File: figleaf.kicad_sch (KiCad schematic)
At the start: 0 parts

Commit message: testing llmd mcu
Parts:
- added J1: nRF52840_Connect_Kit, symbol kekw:nRF52840_Connect_Kit
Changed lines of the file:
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@@
 	(generator_version "9.0")
 	(paper "A4")
+	(symbol
+		(lib_id "kekw:nRF52840_Connect_Kit")
+		(at 166.37 91.44 0)
+		(unit 1)
+		(exclude_from_sim no)
+		(in_bom yes)
+		(on_board yes)
+		(dnp no)
+		(fields_autoplaced yes)
+		(property "Reference" "J1"
+			(at 166.37 35.56 0)
+			(effects
+				(font
+					(size 1.27 1.27)
+				)
+			)
+		)
+		(property "Value" "nRF52840_Connect_Kit"
+			(at 166.37 38.1 0)
+			(effects
+				(font
+					(size 1.27 1.27)
+				)
+			)
+		)
+		(property "Footprint" ""
+			(at 166.37 91.44 0)
+			(effects
+				(font
+					(size 1.27 1.27)
+				)
+				(hide yes)
+			)
+		)
+		(property "Datasheet" ""
+			(at 166.37 91.44 0)
+			(effects
+				(font
+					(size 1.27 1.27)
+				)
+				(hide yes)
+			)
+		)
+		(property "Description" "nRF52840 Connect Kit 2x20 Header"
+			(at 166.37 91.44 0)
+			(effects
+				(font
+					(size 1.27 1.27)
+				)
+				(hide yes)
+			)
+		)
+		(pin "40"
+		)
+		(pin "14"
+		)
+		(pin "3"
+		)
+		(pin "7"
+		)
+		(pin "15"
+		)
+		(pin "17"
+		)
+		(pin "20"
+		)
+		(pin "30"
+		)
+		(pin "1"
+		)
+		(pin "10"
+		)
+		(pin "12"
+		)
+		(pin "16"
+		)
+		(pin "11"
+		)
+		(pin "39"
+		)
+		(pin "10"
+		)
+		(pin "38"
+		)
+		(pin "6"
+		)
+		(pin "4"
+		)
+		(pin "18"
+		)
+		(pin "2"
+		)
+		(pin "8"
+		)
+		(pin "9"
+		)
+		(pin "13"
+		)
+		(pin "5"
+		)
+		(pin "19"
+		)
+		(pin "37"
+		)
+		(pin "35"
+		)
+		(pin "34"
+		)
+		(pin "36"
+		)
+		(pin "33"
+		)
+		(pin "32"
+		)
+		(pin "31"
+		)
+		(pin "28"
+		)
+		(pin "29"
+		)
+		(pin "22"
+		)
+		(pin "25"
+		)
+		(pin "24"
+		)
+		(pin "26"
+		)
+		(pin "23"
+		)
+		(pin "27"
+		)
+		(pin "21"
+		)
+		(instances
+			(project ""
+				(path "/fd9c0cf8-91e7-46bd-8f73-27ef3bc34e44"
+					(reference "J1")
+					(unit 1)
+				)
+			)
+		)
+	)
 	(sheet_instances
 		(path "/"

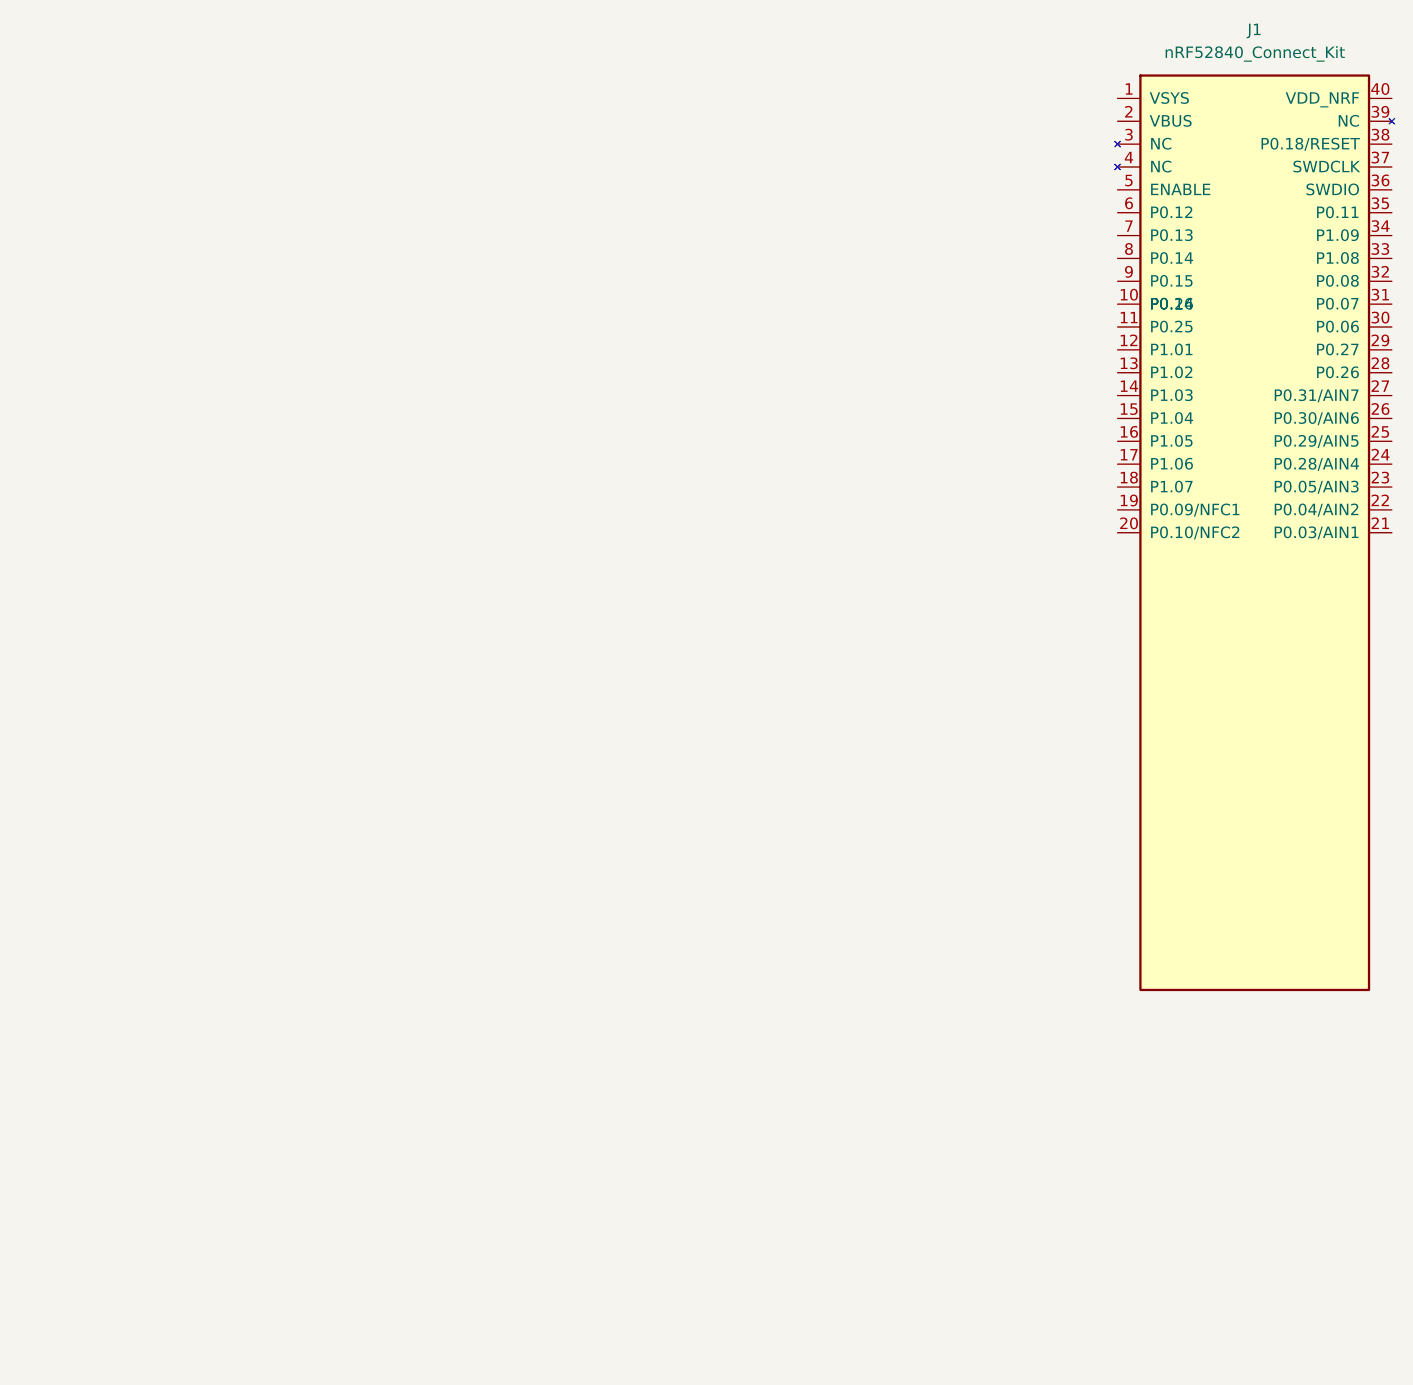
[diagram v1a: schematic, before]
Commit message: Add proper MCU symbol
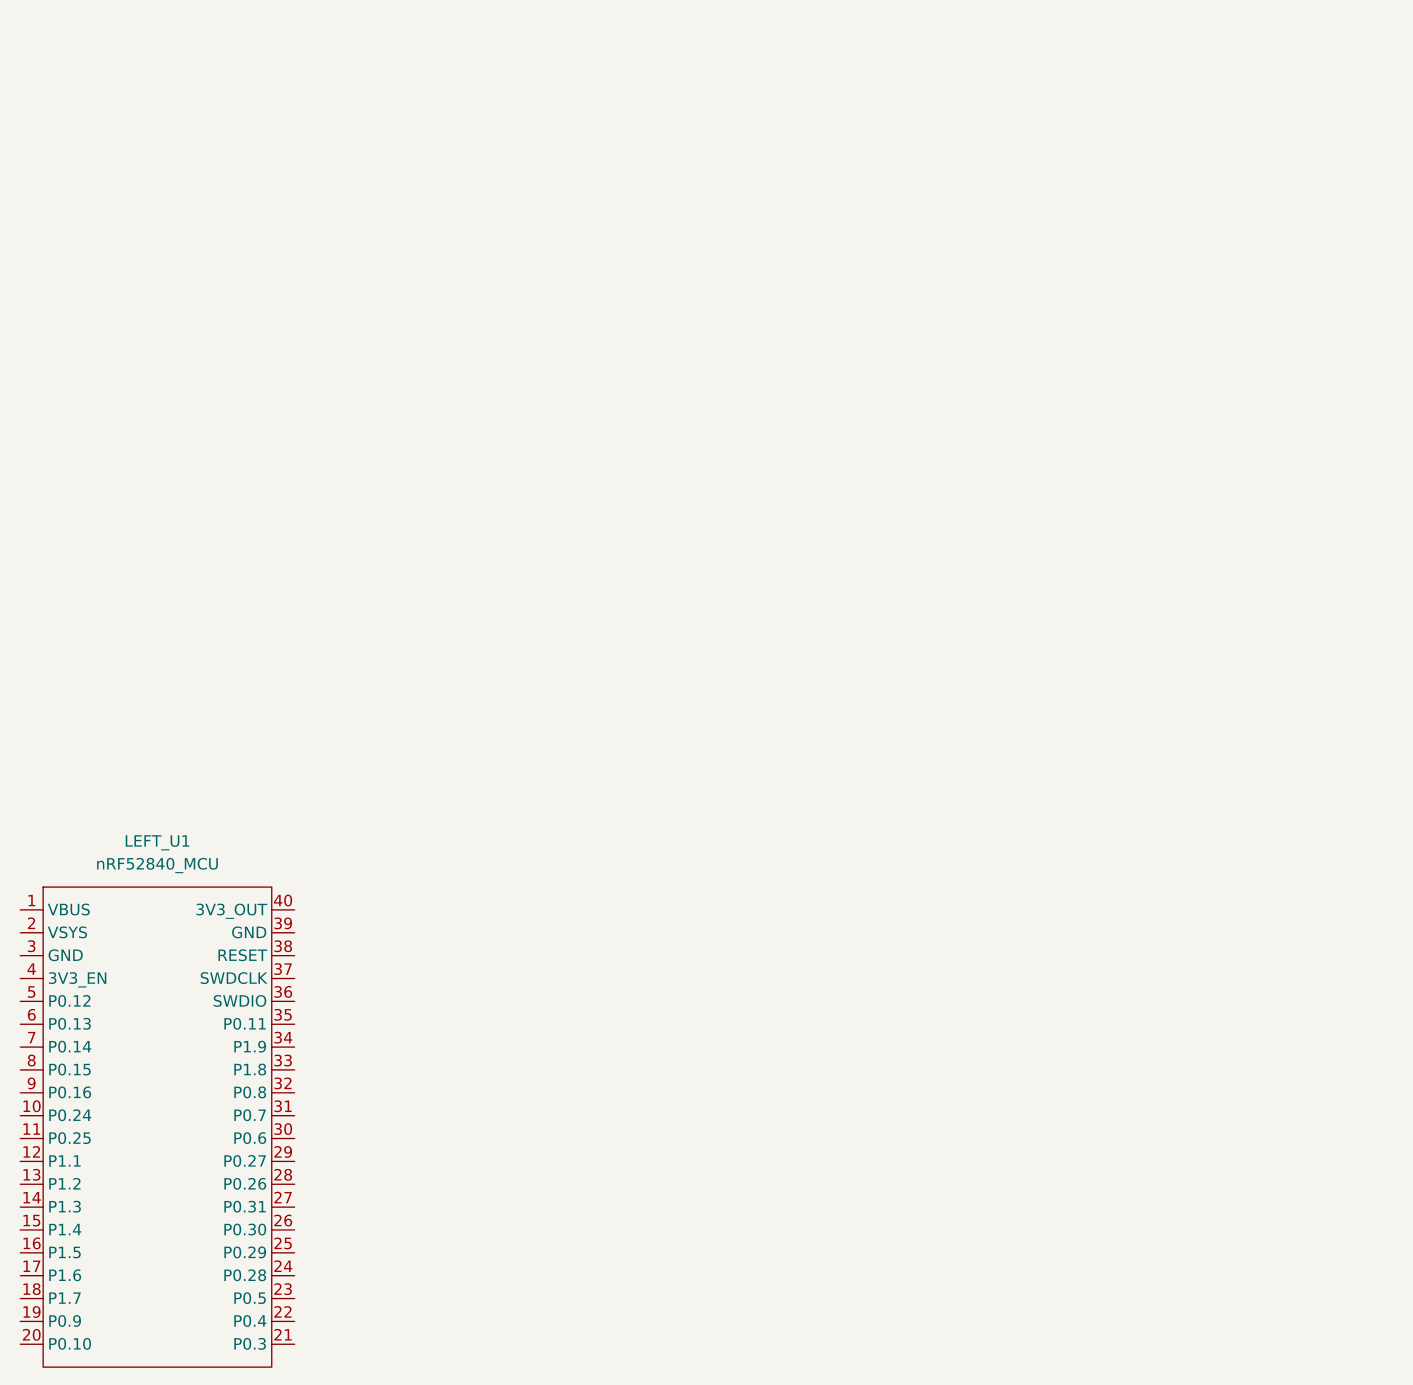
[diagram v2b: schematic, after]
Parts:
- removed J1: nRF52840_Connect_Kit, symbol kekw:nRF52840_Connect_Kit
- added LEFT_U1: nRF52840_MCU, symbol 0_graz_symbols:nRF52840_MCU
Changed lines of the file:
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@@
 	(paper "A4")
 	(symbol
-		(lib_id "kekw:nRF52840_Connect_Kit")
-		(at 166.37 91.44 0)
+		(lib_id "0_graz_symbols:nRF52840_MCU")
+		(at 44.45 158.75 0)
 		(unit 1)
 		(exclude_from_sim no)
@@
 		(dnp no)
 		(fields_autoplaced yes)
-		(property "Reference" "J1"
-			(at 166.37 35.56 0)
+		(property "Reference" "LEFT_U1"
+			(at 44.45 125.73 0)
 			(effects
 				(font
@@
 			)
 		)
-		(property "Value" "nRF52840_Connect_Kit"
-			(at 166.37 38.1 0)
+		(property "Value" "nRF52840_MCU"
+			(at 44.45 128.27 0)
 			(effects
 				(font
@@
 		)
 		(property "Footprint" ""
-			(at 166.37 91.44 0)
+			(at 44.45 158.75 0)
 			(effects
 				(font
@@
 		)
 		(property "Datasheet" ""
-			(at 166.37 91.44 0)
+			(at 44.45 158.75 0)
 			(effects
 				(font
@@
 			)
 		)
-		(property "Description" "nRF52840 Connect Kit 2x20 Header"
-			(at 166.37 91.44 0)
+		(property "Description" ""
+			(at 44.45 158.75 0)
 			(effects
 				(font
@@
 			)
 		)
-		(pin "40"
+		(pin "24"
+		)
+		(pin "31"
+		)
+		(pin "16"
+		)
+		(pin "28"
+		)
+		(pin "27"
+		)
+		(pin "25"
+		)
+		(pin "35"
+		)
+		(pin "39"
+		)
+		(pin "19"
 		)
 		(pin "14"
 		)
-		(pin "3"
+		(pin "20"
 		)
-		(pin "7"
+		(pin "40"
 		)
 		(pin "15"
@@
 		(pin "17"
 		)
-		(pin "20"
-		)
-		(pin "30"
-		)
-		(pin "1"
-		)
-		(pin "10"
-		)
-		(pin "12"
-		)
-		(pin "16"
-		)
-		(pin "11"
-		)
-		(pin "39"
-		)
-		(pin "10"
+		(pin "13"
 		)
 		(pin "38"
 		)
-		(pin "6"
-		)
-		(pin "4"
-		)
-		(pin "18"
-		)
-		(pin "2"
-		)
-		(pin "8"
-		)
-		(pin "9"
-		)
-		(pin "13"
-		)
-		(pin "5"
-		)
-		(pin "19"
+		(pin "34"
 		)
 		(pin "37"
-		)
-		(pin "35"
-		)
-		(pin "34"
 		)
 		(pin "36"
@@
 		(pin "32"
 		)
-		(pin "31"
+		(pin "18"
 		)
-		(pin "28"
+		(pin "30"
 		)
 		(pin "29"
-		)
-		(pin "22"
-		)
-		(pin "25"
-		)
-		(pin "24"
 		)
 		(pin "26"
@@
 		(pin "23"
 		)
-		(pin "27"
+		(pin "21"
 		)
-		(pin "21"
+		(pin "22"
+		)
+		(pin "2"
+		)
+		(pin "5"
+		)
+		(pin "7"
+		)
+		(pin "10"
+		)
+		(pin "12"
+		)
+		(pin "1"
+		)
+		(pin "4"
+		)
+		(pin "3"
+		)
+		(pin "6"
+		)
+		(pin "8"
+		)
+		(pin "9"
+		)
+		(pin "11"
 		)
 		(instances
 			(project ""
 				(path "/fd9c0cf8-91e7-46bd-8f73-27ef3bc34e44"
-					(reference "J1")
+					(reference "LEFT_U1")
 					(unit 1)
 				)

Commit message: progress on 2x2 test schematics
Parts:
- removed LEFT_U1: nRF52840_MCU, symbol 0_graz_symbols:nRF52840_MCU
- added S1, S2, S3, S4: SW_OKM, symbol 0_graz_symbols:SW_OKM
- added U1: Nice_Nano_V2, ScottoKeebs_MCU:Nice_Nano_V2, symbol 1_scotto_symbols:MCU_Nice_Nano_V2
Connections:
- new net: S2.2 (C-OUT), S4.1 (C-IN)
- new net: S1.4 (R-OUT), S2.3 (R-IN)
- new net: S2.6 (GND), S4.5 (GND)
- new net: S1.2 (C-OUT), S3.1 (C-IN)
- new net: S1.6 (GND), S3.5 (GND)
- new net: S3.4 (R-OUT), S4.3 (R-IN)
- new net GND_L: S3.6 (GND), S4.6 (GND), U1.23 (GND), U1.3 (GND), U1.4 (GND)
- new net RAW_L: U1.24 (B+)
- new net RESET_L: U1.22 (RST)
- new net col_0: S1.1 (C-IN), U1.5 (2)
- new net col_1: S2.1 (C-IN), U1.6 (3)
- new net row_0: S1.3 (R-IN), U1.20 (21)
- new net row_1: S3.3 (R-IN), U1.19 (20)
- no-connect marks 0 -> 4

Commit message: kicad progress
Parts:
- S1, S2, S3, S4: footprint (none) -> Graz_Footprints:One Key Module
- U1: footprint ScottoKeebs_MCU:Nice_Nano_V2 -> MCU:Nice_Nano_V2
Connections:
- net col_0: now also U1.20 (21); no longer U1.5 (2)
- net col_1: now also U1.19 (20); no longer U1.6 (3)
- net row_0: now also S2.4 (R-OUT), U1.5 (2); no longer S1.3 (R-IN), U1.20 (21)
- net row_1: now also S4.4 (R-OUT), U1.6 (3); no longer S3.3 (R-IN), U1.19 (20)
- no-connect marks 4 -> 0
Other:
- moved on the sheet: S1, S2, S3, S4, U1

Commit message: progress pcb
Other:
- moved on the sheet: S1, S2, S3, S4, U1
